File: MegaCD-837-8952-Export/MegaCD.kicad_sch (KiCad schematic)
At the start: 182 parts, among them CN1 CON 25P ANGLE, CN2 EDGE 60P, CN3 CON 21P, IC1 68HC000, IC10 65256BLFP-10T, IC11 65256BLFP-10T, IC12 74HC86, IC13 LC8951, IC14 MB8464A-90L, IC15 MB8464A-90L, IC16 MB8464A-10L, IC17 74AC74, IC2 315-5548/315-5632, IC3 315-5476A, IC4 27C1024, IC5 HM514270, IC6 MB3790, IC7 TC511664BZ, IC8 TC511664BZ, IC9 74HC245, J2 2TS, J3 MH, J4 CAS0, M0 TestPoint, M1 TestPoint, M10 TestPoint, M11 TestPoint, M12 TestPoint, M13 TestPoint, M14 TestPoint, M192 TestPoint, M2 TestPoint, M3 TestPoint, M4 TestPoint, M5 TestPoint, M57 TestPoint, M6 TestPoint, M7 TestPoint, M8 TestPoint, M9 TestPoint

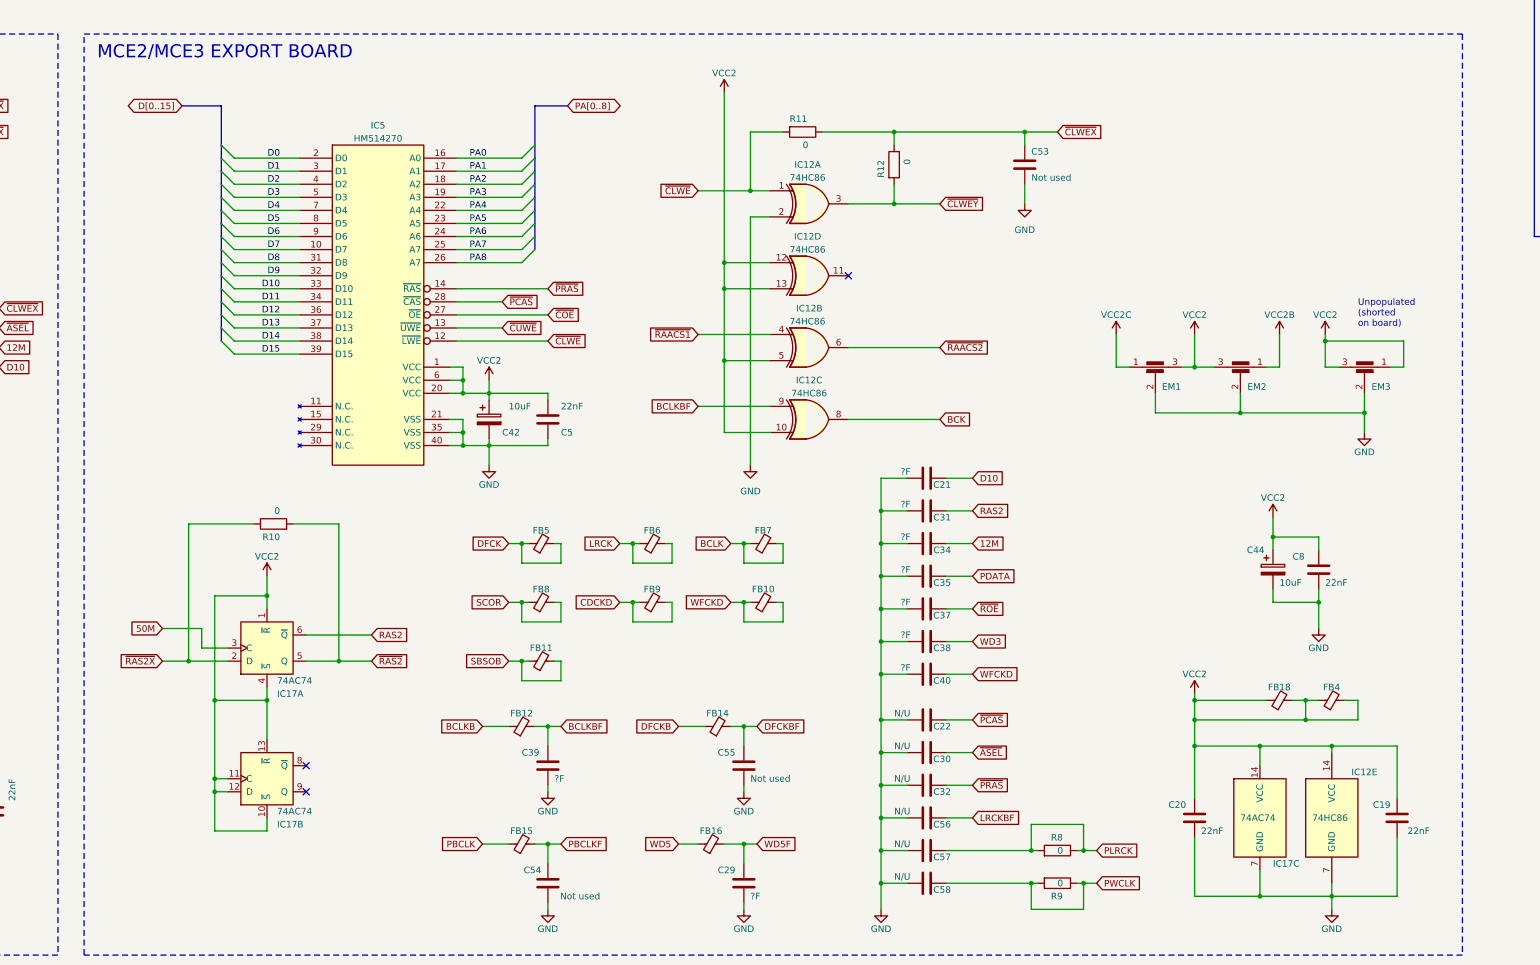
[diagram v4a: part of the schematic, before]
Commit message: Add measured capacitor values and tidy schematic for export board.
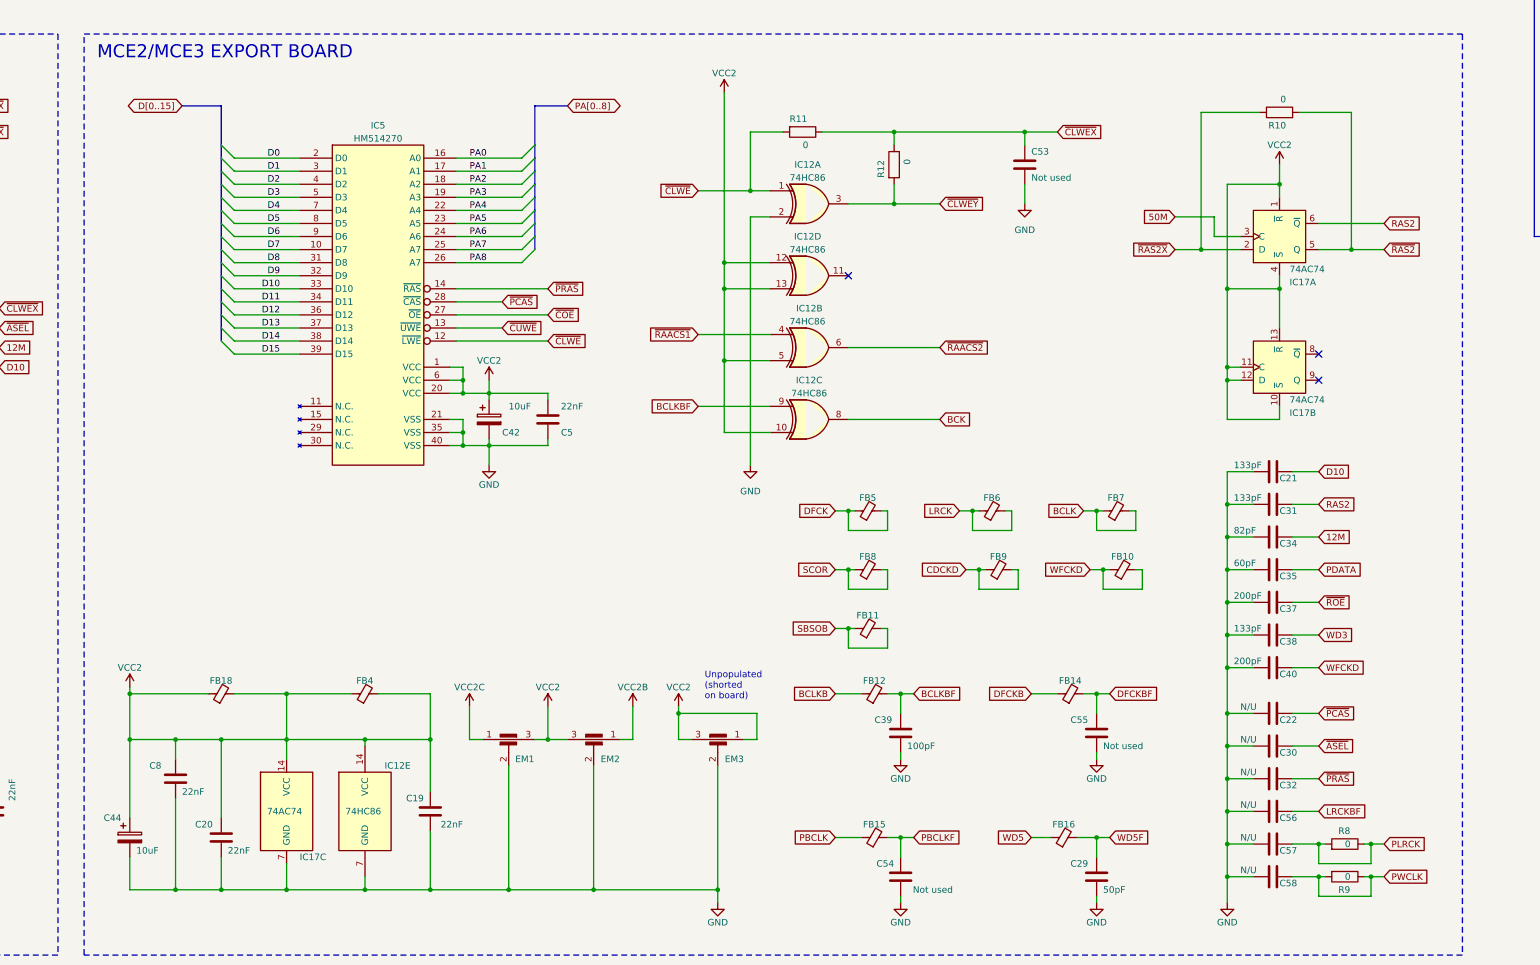
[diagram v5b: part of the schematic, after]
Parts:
- C21, C31, C38: value ?F -> 133pF
- C29: value ?F -> 50pF
- C34: value ?F -> 82pF
- C35: value ?F -> 60pF
- C37, C40: value ?F -> 200pF
- C39: value ?F -> 100pF
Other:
- moved on the sheet: C19, C20, C21, C22, C29, C30, C31, C32, C34, C35, C37, C38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

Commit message: Update README
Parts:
- C1: value 1000pF -> 1uF
- C21: value 133pF -> 100pF
- C24, C27: value Not used -> 100pF
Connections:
- net ~{CLWEY}: no longer names the net of IC12.3, R12.2
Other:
- moved on the sheet: C53
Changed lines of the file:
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@@
   (junction (at 350.52 535.94) (diameter 0) (color 0 0 0 0)
   )
-  (junction (at 494.03 417.83) (diameter 0) (color 0 0 0 0)
+  (junction (at 482.6 417.83) (diameter 0) (color 0 0 0 0)
   )
   (junction (at 185.42 134.62) (diameter 0) (color 0 0 0 0)
@@
   (junction (at 508 527.05) (diameter 0) (color 0 0 0 0)
   )
-  (junction (at 468.63 431.8) (diameter 0) (color 0 0 0 0)
-  )
   (junction (at 533.4 502.92) (diameter 0) (color 0 0 0 0)
   )
@@
     (stroke (width 0) (type default))
   )
-  (wire (pts (xy 494.03 417.83) (xy 494.03 420.37))
+  (wire (pts (xy 482.6 417.83) (xy 482.6 420.37))
     (stroke (width 0) (type default))
   )
@@
     (stroke (width 0) (type default))
   )
-  (wire (pts (xy 494.03 417.83) (xy 500.38 417.83))
+  (wire (pts (xy 482.6 417.83) (xy 488.95 417.83))
     (stroke (width 0) (type default))
   )
@@
     (stroke (width 0) (type default))
   )
-  (wire (pts (xy 468.63 431.8) (xy 477.52 431.8))
-    (stroke (width 0) (type default))
-  )
   (wire (pts (xy 238.76 516.89) (xy 236.22 516.89))
     (stroke (width 0) (type default))
@@
     (stroke (width 0) (type default))
   )
-  (wire (pts (xy 468.63 417.83) (xy 494.03 417.83))
+  (wire (pts (xy 468.63 417.83) (xy 482.6 417.83))
     (stroke (width 0) (type default))
   )
@@
     (stroke (width 0) (type default))
   )
-  (wire (pts (xy 494.03 427.99) (xy 494.03 431.8))
+  (wire (pts (xy 482.6 427.99) (xy 482.6 431.8))
     (stroke (width 0) (type default))
   )
@@
     (effects (font (size 1.27 1.27)) (justify right bottom))
   )
+  (text "Extra decoupling IC2" (at 325.12 560.07 90)
+    (effects (font (size 1.27 1.27)) (justify left bottom))
+  )
   (text "GREY" (at 193.04 494.03 0)
     (effects (font (size 1.27 1.27)) (justify right bottom))
@@
     )
   )
-  (global_label "~{CLWEY}" (shape input) (at 477.52 431.8 0) (fields_autoplaced)
-    (effects (font (size 1.27 1.27)) (justify left))
-    (property "Intersheetrefs" "${INTERSHEET_REFS}" (at 486.4129 431.8 0)
-      (effects (font (size 1.27 1.27)) (justify left) hide)
-    )
-  )
   (global_label "WFCK" (shape input) (at 711.2 214.63 0) (fields_autoplaced)
     (effects (font (size 1.27 1.27)) (justify left))
@@
     )
   )
-  (global_label "~{CLWEX}" (shape input) (at 500.38 417.83 0) (fields_autoplaced)
+  (global_label "~{CLWEX}" (shape input) (at 488.95 417.83 0) (fields_autoplaced)
     (effects (font (size 1.27 1.27)) (justify left))
-    (property "Intersheetrefs" "${INTERSHEET_REFS}" (at 509.3938 417.83 0)
+    (property "Intersheetrefs" "${INTERSHEET_REFS}" (at 497.9638 417.83 0)
       (effects (font (size 1.27 1.27)) (justify left) hide)
     )
@@
       (effects (font (size 1.27 1.27)) (justify left))
     )
-    (property "Value" "133pF" (at 534.67 482.6 90)
+    (property "Value" "100pF" (at 534.67 482.6 90)
       (effects (font (size 1.27 1.27)) (justify left))
     )
@@
       (effects (font (size 1.27 1.27)) (justify left))
     )
-    (property "Value" "Not used" (at 758.19 165.1 90)
+    (property "Value" "100pF" (at 758.19 165.1 90)
       (effects (font (size 1.27 1.27)) (justify left))
     )
@@
     )
   )
-  (symbol (lib_id "Device:C") (at 494.03 424.18 0) (unit 1)
+  (symbol (lib_id "Device:C") (at 482.6 424.18 0) (unit 1)
     (in_bom yes) (on_board yes) (dnp no)
-    (property "Reference" "C53" (at 495.3 421.64 0)
+    (property "Reference" "C53" (at 483.87 421.64 0)
       (effects (font (size 1.27 1.27)) (justify left))
     )
-    (property "Value" "Not used" (at 495.3 426.72 0)
+    (property "Value" "Not used" (at 483.87 426.72 0)
       (effects (font (size 1.27 1.27)) (justify left))
     )
-    (property "Footprint" "MegaCD_Footprints:SMD_0805_HandSolder" (at 494.9952 427.99 0)
+    (property "Footprint" "MegaCD_Footprints:SMD_0805_HandSolder" (at 483.5652 427.99 0)
       (effects (font (size 1.27 1.27)) hide)
     )
-    (property "Datasheet" "~" (at 494.03 424.18 0)
+    (property "Datasheet" "~" (at 482.6 424.18 0)
       (effects (font (size 1.27 1.27)) hide)
     )
@@
       (effects (font (size 1.27 1.27)) (justify left))
     )
-    (property "Value" "10uF" (at 321.31 557.53 0)
+    (property "Value" "10uF" (at 314.96 558.8 0)
       (effects (font (size 1.27 1.27)) (justify left))
     )
@@
   (symbol (lib_id "Device:C") (at 328.93 543.56 0) (unit 1)
     (in_bom yes) (on_board yes) (dnp no)
-    (property "Reference" "C8" (at 323.85 541.02 0)
+    (property "Reference" "C8" (at 330.2 541.02 0)
       (effects (font (size 1.27 1.27)) (justify left))
     )
@@
       (effects (font (size 1.27 1.27)) (justify left))
     )
-    (property "Value" "1000pF" (at 55.88 67.31 0)
+    (property "Value" "1uF" (at 58.42 67.31 0)
       (effects (font (size 1.27 1.27)) (justify left))
     )
@@
       (effects (font (size 1.27 1.27)) (justify left))
     )
-    (property "Value" "Not used" (at 814.07 121.92 90)
+    (property "Value" "100pF" (at 814.07 121.92 90)
       (effects (font (size 1.27 1.27)) (justify left))
     )
@@
     )
   )
-  (symbol (lib_id "power:GND") (at 494.03 431.8 0) (unit 1)
+  (symbol (lib_id "power:GND") (at 482.6 431.8 0) (unit 1)
     (in_bom yes) (on_board yes) (dnp no) (fields_autoplaced)
-    (property "Reference" "#PWR081" (at 494.03 438.15 0)
+    (property "Reference" "#PWR081" (at 482.6 438.15 0)
       (effects (font (size 1.27 1.27)) hide)
     )
-    (property "Value" "GND" (at 494.03 436.88 0)
+    (property "Value" "GND" (at 482.6 436.88 0)
       (effects (font (size 1.27 1.27)))
     )
-    (property "Footprint" "" (at 494.03 431.8 0)
+    (property "Footprint" "" (at 482.6 431.8 0)
       (effects (font (size 1.27 1.27)) hide)
     )
-    (property "Datasheet" "" (at 494.03 431.8 0)
+    (property "Datasheet" "" (at 482.6 431.8 0)
       (effects (font (size 1.27 1.27)) hide)
     )

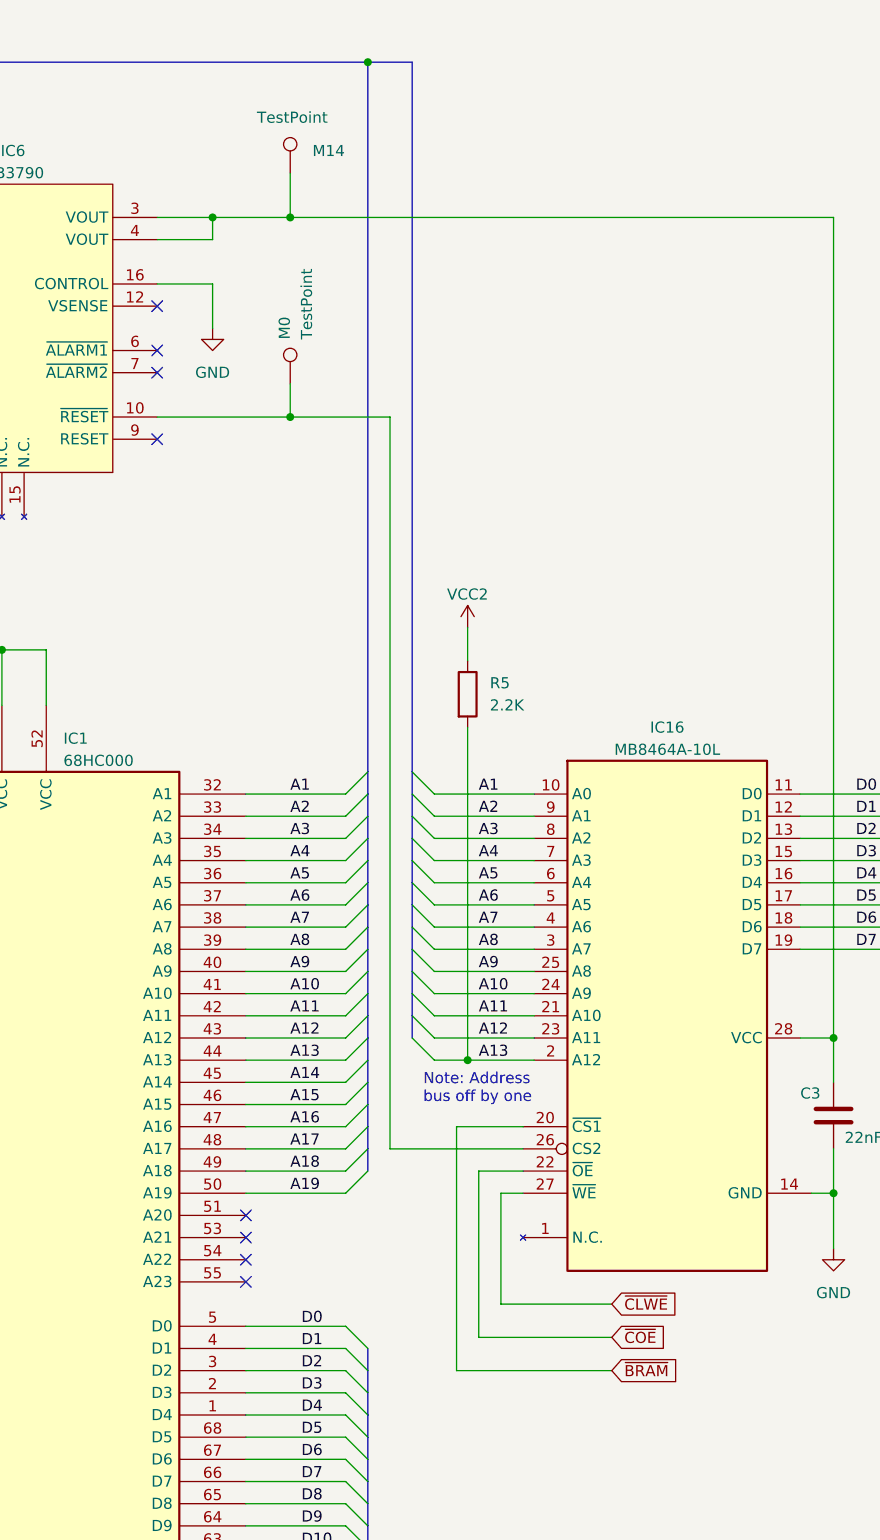
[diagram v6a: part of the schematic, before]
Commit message: Implement FRAM size jumpers for 837-8952-Export.
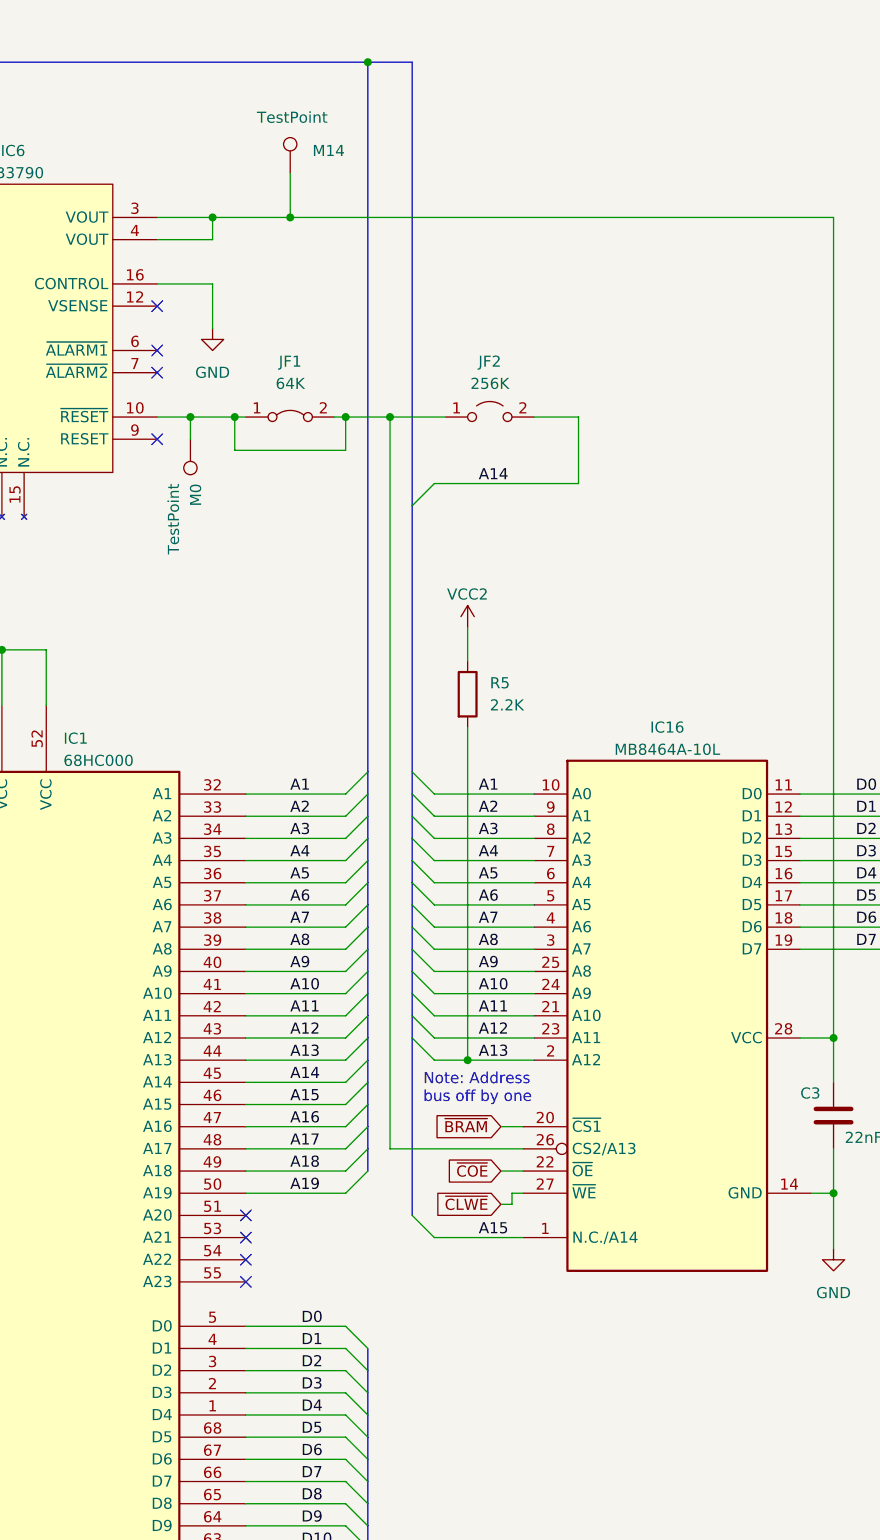
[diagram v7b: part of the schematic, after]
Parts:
- added JF1: 64K, MegaCD_Footprints:SMD_0805_HandSolder, symbol Jumper:Jumper_2_Bridged
- added JF2: 256K, MegaCD_Footprints:SMD_0805_HandSolder, symbol Jumper:Jumper_2_Open
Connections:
- net A14: now also JF2.2 (B)
- net A15: now also IC16.1 (N.C./A14)
- net at IC16.26 (CS2/A13), IC6.10 (~{RESET}), M0.1: now also JF1.1 (A), JF1.2 (B), JF2.1 (A)
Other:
- moved on the sheet: M0
